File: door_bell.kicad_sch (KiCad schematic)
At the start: 75 parts, among them J1 8-10V AC/DC, J2 Speaker, J3 SWITCH1, J4 Door panel, J5 UART, J6 JTAG, J7 BOOT, J8 MicroSD, K1 HJR 1-2C, Q1 BC338, SW1 Reset, U1 NCP1117-5v, U2 MAX98357A, U3 NCP1117-3v3, U4 DS3231M, U5 MAX3232, U6 ESP32-WROVER-B, U7 74LVC2G14

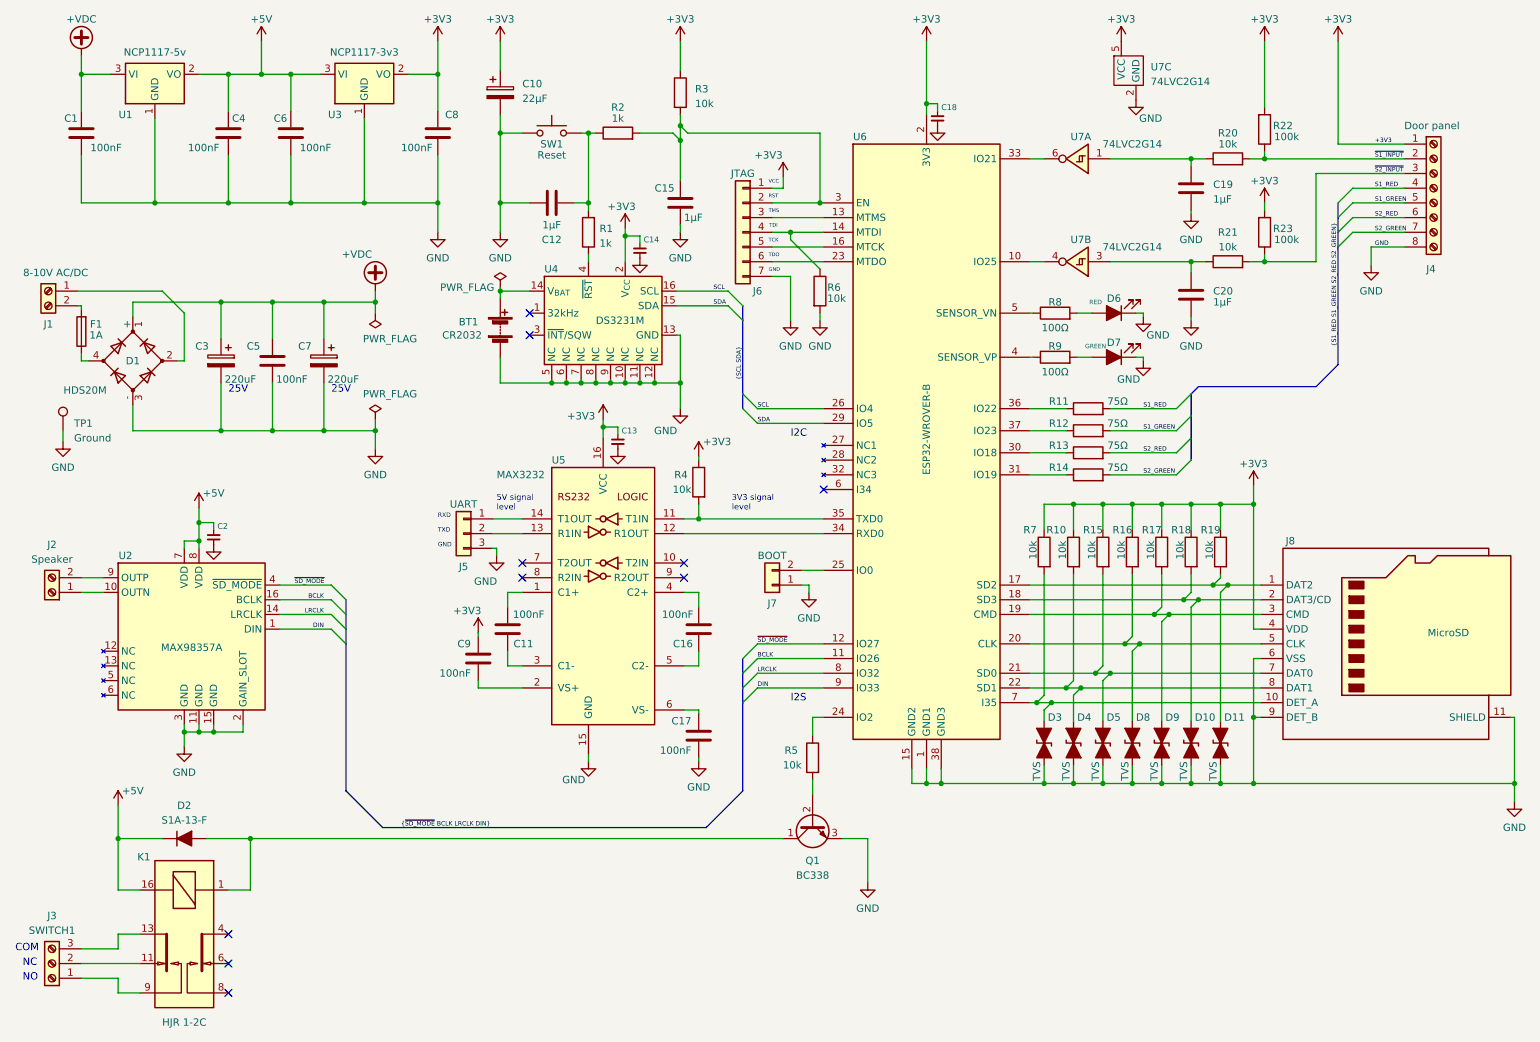
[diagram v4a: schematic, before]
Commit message: GND plane routing
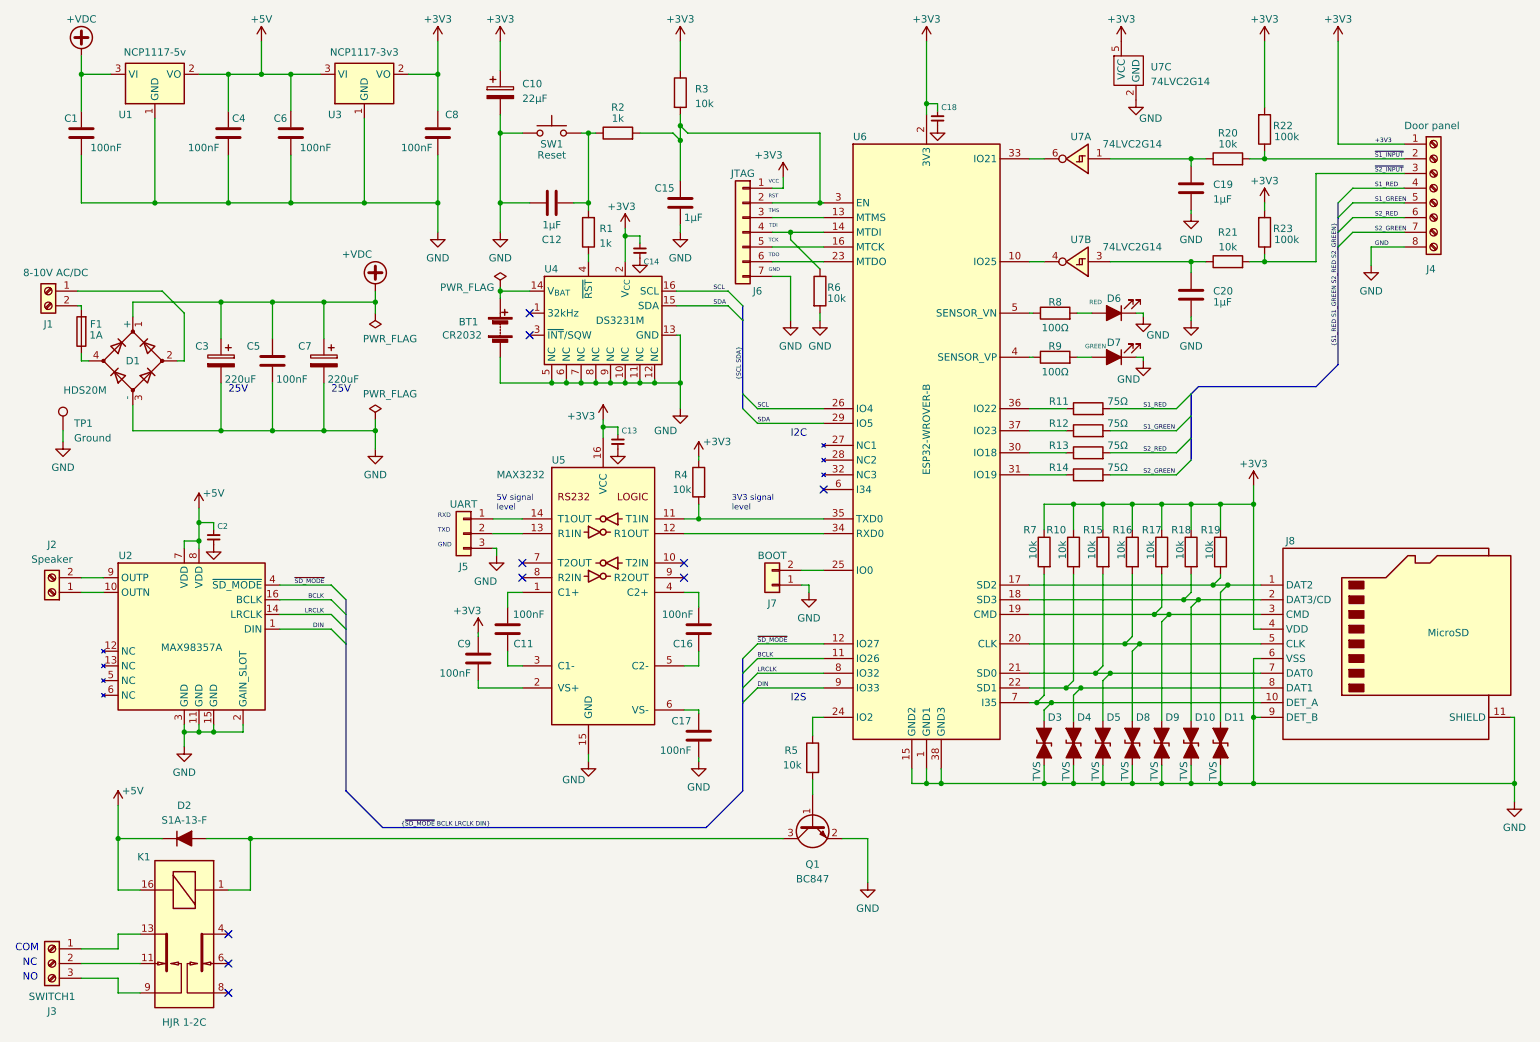
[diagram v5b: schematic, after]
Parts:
- removed Q1: BC338, Package_TO_SOT_THT:TO-92_Inline, symbol Transistor_BJT:BC338
- added Q1: BC847, Package_TO_SOT_SMD:SOT-23, symbol Transistor_BJT:BC847
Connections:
- net +3V3: now also C14.2; no longer C14.1
- net GND: now also C14.1, Q1.2 (E); no longer C14.2
- net at D2.2 (A), K1.1: now also Q1.3 (C)
- net at K1.13: now also J3.1 (Pin_1); no longer J3.3 (Pin_3)
- net at K1.9: now also J3.3 (Pin_3); no longer J3.1 (Pin_1)
- net at R5.2: now also Q1.1 (B)
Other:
- moved on the sheet: J3
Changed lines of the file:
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@@
     )
   )
-  (symbol (lib_id "Connector:Screw_Terminal_01x03") (at 25.4 182.245 180) (unit 1)
-    (in_bom yes) (on_board yes) (dnp no) (fields_autoplaced)
-    (property "Reference" "J3" (at 25.4 173.99 0)
-      (effects (font (size 1.27 1.27)))
-    )
-    (property "Value" "SWITCH1" (at 25.4 176.53 0)
+  (symbol (lib_id "Connector:Screw_Terminal_01x03") (at 25.4 182.245 0) (mirror y) (unit 1)
+    (in_bom yes) (on_board yes) (dnp no)
+    (property "Reference" "J3" (at 25.4 190.5 0)
+      (effects (font (size 1.27 1.27)))
+    )
+    (property "Value" "SWITCH1" (at 25.4 187.96 0)
       (effects (font (size 1.27 1.27)))
     )
@@
         (path "/c78ad4c4-54c1-4b1d-a971-e4b8abed6bf8"
           (reference "R3") (unit 1)
-        )
-      )
-    )
-  )
-  (symbol (lib_id "Transistor_BJT:BC338") (at 156.845 158.115 90) (mirror x) (unit 1)
-    (in_bom yes) (on_board yes) (dnp no) (fields_autoplaced)
-    (property "Reference" "Q1" (at 156.845 164.465 90)
-      (effects (font (size 1.27 1.27)))
-    )
-    (property "Value" "BC338" (at 156.845 167.005 90)
-      (effects (font (size 1.27 1.27)))
-    )
-    (property "Footprint" "Package_TO_SOT_THT:TO-92_Inline" (at 158.75 163.195 0)
-      (effects (font (size 1.27 1.27) italic) (justify left) hide)
-    )
-    (property "Datasheet" "http://diotec.com/tl_files/diotec/files/pdf/datasheets/bc337" (at 156.845 158.115 0)
-      (effects (font (size 1.27 1.27)) (justify left) hide)
-    )
-    (pin "1")
-    (pin "2")
-    (pin "3")
-    (instances
-      (project "door_bell"
-        (path "/c78ad4c4-54c1-4b1d-a971-e4b8abed6bf8"
-          (reference "Q1") (unit 1)
         )
       )
@@
     )
   )
-  (symbol (lib_id "Device_espena:C_Decoupling") (at 127 59.055 0) (unit 1)
-    (in_bom yes) (on_board yes) (dnp no)
-    (property "Reference" "C14" (at 127.635 57.15 0)
+  (symbol (lib_id "Device_espena:C_Decoupling") (at 127 59.055 0) (mirror x) (unit 1)
+    (in_bom yes) (on_board yes) (dnp no)
+    (property "Reference" "C14" (at 127.635 60.96 0)
       (effects (font (size 1 1)) (justify left))
     )
-    (property "Value" "C_Decoupling" (at 127.254 61.087 0)
+    (property "Value" "C_Decoupling" (at 127.254 57.023 0)
       (effects (font (size 1.27 1.27)) (justify left) hide)
     )
@@
         )
       )
+    )
+  )
+  (symbol (lib_id "Transistor_BJT:BC847") (at 156.845 158.115 90) (mirror x) (unit 1)
+    (in_bom yes) (on_board yes) (dnp no) (fields_autoplaced)
+    (property "Reference" "Q1" (at 156.845 165.1 90)
+      (effects (font (size 1.27 1.27)))
+    )
+    (property "Value" "BC847" (at 156.845 167.64 90)
+      (effects (font (size 1.27 1.27)))
+    )
+    (property "Footprint" "Package_TO_SOT_SMD:SOT-23" (at 158.75 163.195 0)
+      (effects (font (size 1.27 1.27) italic) (justify left) hide)
+    )
+    (property "Datasheet" "http://www.infineon.com/dgdl/Infineon-BC847SERIES_BC848SERIES_BC849SERIES_BC850SERIES-DS-v01_01-en.pdf?fileId=db3a304314dca389011541d4630a1657" (at 156.845 158.115 0)
+      (effects (font (size 1.27 1.27)) (justify left) hide)
+    )
+    (pin "1")
+    (pin "2")
+    (pin "3")
+    (instances
+      (project "door_bell"
+        (path "/c78ad4c4-54c1-4b1d-a971-e4b8abed6bf8"
+          (reference "Q1") (unit 1)
+        )
+      )

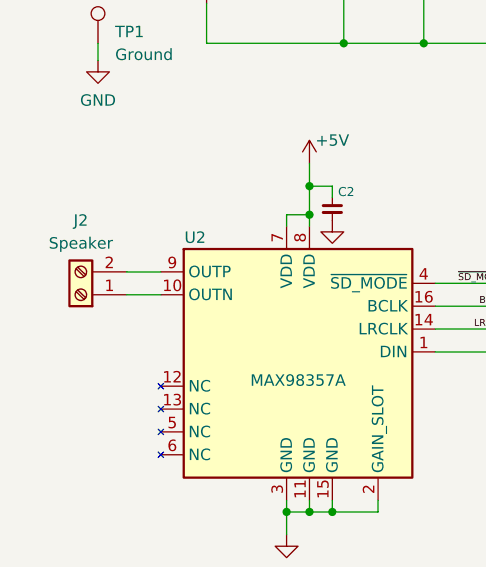
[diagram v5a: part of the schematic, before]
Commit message: Initial routing of power rails and some signals
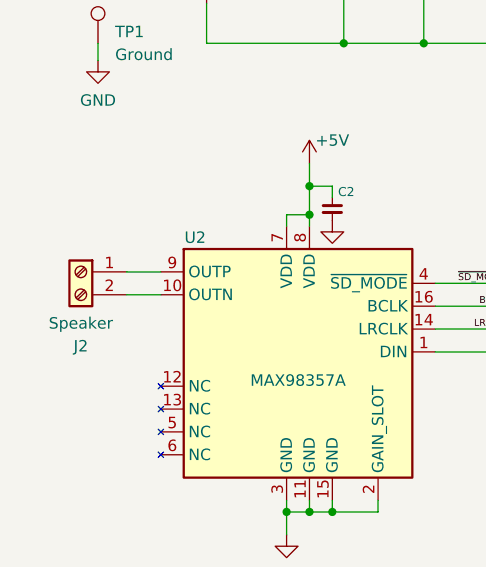
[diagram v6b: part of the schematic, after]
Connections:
- net at J2.1 (Pin_1): now also U2.9 (OUTP); no longer U2.10 (OUTN)
- net at J2.2 (Pin_2): now also U2.10 (OUTN); no longer U2.9 (OUTP)
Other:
- moved on the sheet: J2
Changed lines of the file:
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@@
     )
   )
-  (symbol (lib_id "Connector:Screw_Terminal_01x02") (at 25.4 118.11 180) (unit 1)
-    (in_bom yes) (on_board yes) (dnp no) (fields_autoplaced)
-    (property "Reference" "J2" (at 25.4 109.855 0)
+  (symbol (lib_id "Connector:Screw_Terminal_01x02") (at 25.4 115.57 0) (mirror y) (unit 1)
+    (in_bom yes) (on_board yes) (dnp no)
+    (property "Reference" "J2" (at 25.4 123.825 0)
       (effects (font (size 1.27 1.27)))
     )
-    (property "Value" "Speaker" (at 25.4 112.395 0)
+    (property "Value" "Speaker" (at 25.4 121.285 0)
       (effects (font (size 1.27 1.27)))
     )
-    (property "Footprint" "TerminalBlock_Phoenix:TerminalBlock_Phoenix_PT-1,5-2-3.5-H_1x02_P3.50mm_Horizontal" (at 25.4 118.11 0)
+    (property "Footprint" "TerminalBlock_Phoenix:TerminalBlock_Phoenix_PT-1,5-2-3.5-H_1x02_P3.50mm_Horizontal" (at 25.4 115.57 0)
       (effects (font (size 1.27 1.27)) hide)
     )
-    (property "Datasheet" "~" (at 25.4 118.11 0)
+    (property "Datasheet" "~" (at 25.4 115.57 0)
       (effects (font (size 1.27 1.27)) hide)
     )

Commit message: Done routing
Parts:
- J1, J2: footprint TerminalBlock_Phoenix:TerminalBlock_Phoenix_PT-1,5-2-3.5-H_1x02_P3.50mm_Horizontal -> TerminalBlock_Phoenix_espena:TerminalBlock_Phoenix_PT-1,5-2-3.5-H_1x02_P3.50mm_Horizontal_stackable
- J3: footprint TerminalBlock_Phoenix:TerminalBlock_Phoenix_PT-1,5-3-3.5-H_1x03_P3.50mm_Horizontal -> TerminalBlock_Phoenix_espena:TerminalBlock_Phoenix_PT-1,5-3-3.5-H_1x03_P3.50mm_Horizontal_stackable
- J4: footprint TerminalBlock_Phoenix:TerminalBlock_Phoenix_PT-1,5-8-3.5-H_1x08_P3.50mm_Horizontal -> TerminalBlock_Phoenix_espena:TerminalBlock_Phoenix_PT-1,5-8-3.5-H_1x08_P3.50mm_Horizontal_stackable
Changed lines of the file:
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@@
       (effects (font (size 1.27 1.27)))
     )
-    (property "Footprint" "TerminalBlock_Phoenix:TerminalBlock_Phoenix_PT-1,5-2-3.5-H_1x02_P3.50mm_Horizontal" (at 24.765 66.04 0)
+    (property "Footprint" "TerminalBlock_Phoenix_espena:TerminalBlock_Phoenix_PT-1,5-2-3.5-H_1x02_P3.50mm_Horizontal_stackable" (at 24.765 66.04 0)
       (effects (font (size 1.27 1.27)) hide)
     )
@@
       (effects (font (size 1.27 1.27)) (justify left))
     )
-    (property "Footprint" "TerminalBlock_Phoenix:TerminalBlock_Phoenix_PT-1,5-8-3.5-H_1x08_P3.50mm_Horizontal" (at 264.16 48.26 0)
+    (property "Footprint" "TerminalBlock_Phoenix_espena:TerminalBlock_Phoenix_PT-1,5-8-3.5-H_1x08_P3.50mm_Horizontal_stackable" (at 264.16 48.26 0)
       (effects (font (size 1.27 1.27)) hide)
     )
@@
       (effects (font (size 1.27 1.27)))
     )
-    (property "Footprint" "TerminalBlock_Phoenix:TerminalBlock_Phoenix_PT-1,5-3-3.5-H_1x03_P3.50mm_Horizontal" (at 25.4 182.245 0)
+    (property "Footprint" "TerminalBlock_Phoenix_espena:TerminalBlock_Phoenix_PT-1,5-3-3.5-H_1x03_P3.50mm_Horizontal_stackable" (at 25.4 182.245 0)
       (effects (font (size 1.27 1.27)) hide)
     )
@@
       (effects (font (size 1.27 1.27)))
     )
-    (property "Footprint" "TerminalBlock_Phoenix:TerminalBlock_Phoenix_PT-1,5-2-3.5-H_1x02_P3.50mm_Horizontal" (at 25.4 115.57 0)
-      (effects (font (size 1.27 1.27)) hide)
-    )
+    (property "Footprint" "TerminalBlock_Phoenix_espena:TerminalBlock_Phoenix_PT-1,5-2-3.5-H_1x02_P3.50mm_Horizontal_stackable" (at 25.4 115.57 0)
+      (effects (font (size 1.27 1.27)) hide)
+    )

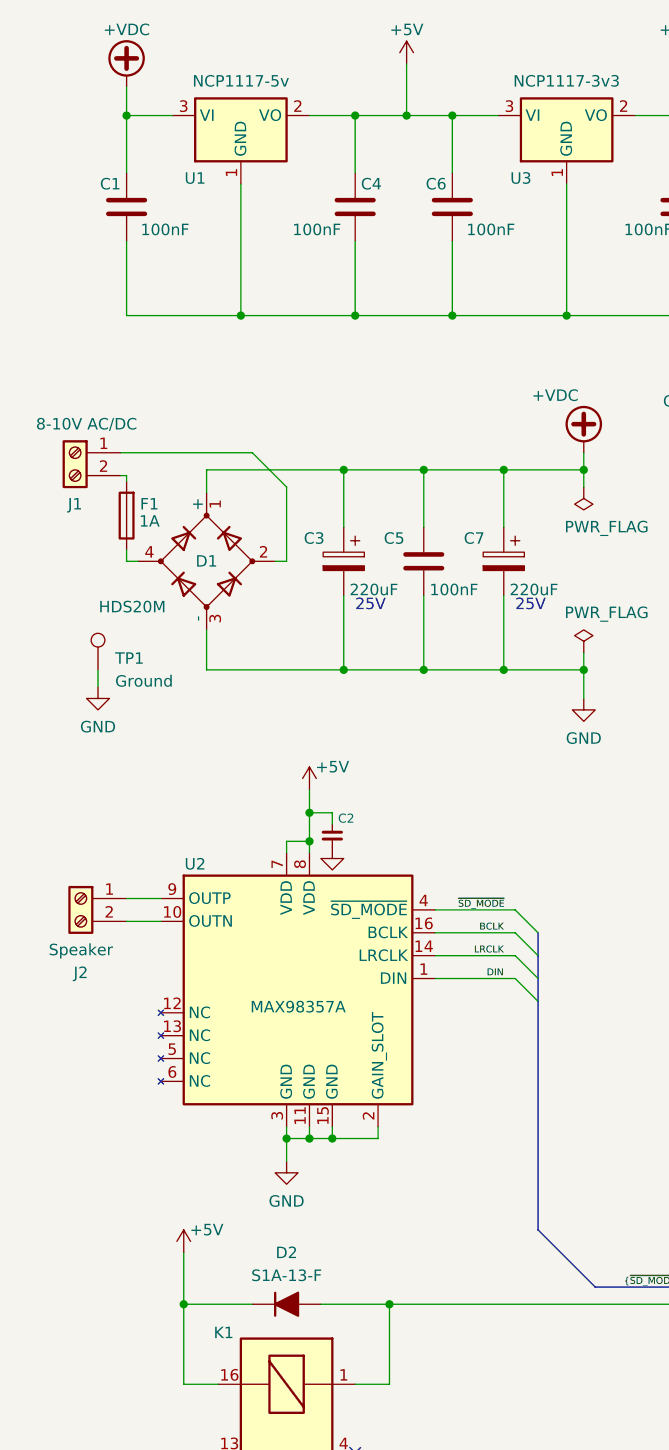
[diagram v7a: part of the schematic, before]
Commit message: Change to alternative voltage regulator types
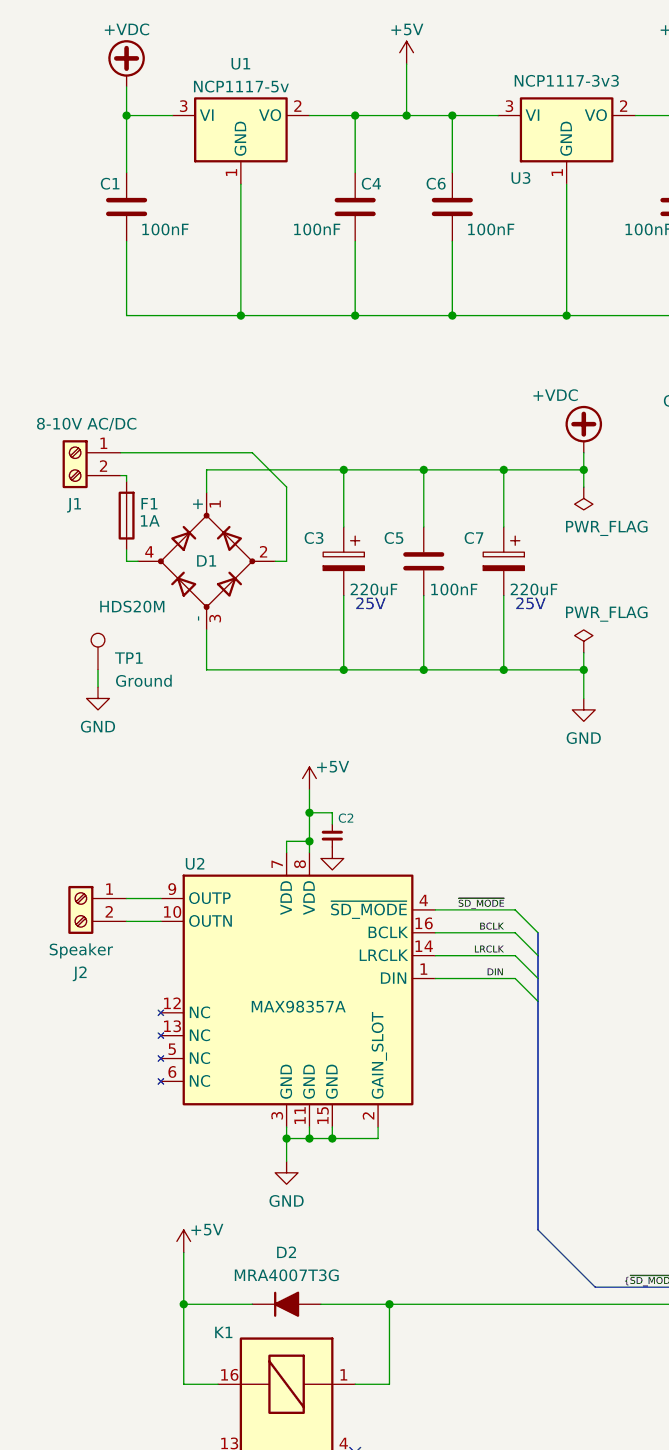
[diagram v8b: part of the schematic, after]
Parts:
- removed U1: NCP1117-5v, Package_TO_SOT_SMD:SOT-223-3_TabPin2, symbol Regulator_Linear:NCP1117-3.3_SOT223
- added U1: NCP1117-5v, Package_TO_SOT_SMD:SOT-223-3_TabPin2, symbol Regulator_Linear:NCP1117-5.0_SOT223
- D2: value S1A-13-F -> MRA4007T3G
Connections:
- net +5V: now also U1.2 (VO)
- net +VDC: now also U1.3 (VI)
- net GND: now also U1.1 (GND)
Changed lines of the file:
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@@
       (effects (font (size 1.27 1.27)))
     )
-    (property "Value" "S1A-13-F" (at 48.26 157.48 0)
+    (property "Value" "MRA4007T3G" (at 48.26 157.48 0)
       (effects (font (size 1.27 1.27)))
     )
@@
         (path "/c78ad4c4-54c1-4b1d-a971-e4b8abed6bf8"
           (reference "R21") (unit 1)
-        )
-      )
-    )
-  )
-  (symbol (lib_id "Regulator_Linear:NCP1117-3.3_SOT223") (at 43.18 28.575 0) (unit 1)
-    (in_bom yes) (on_board yes) (dnp no)
-    (property "Reference" "U1" (at 38.1 35.56 0)
-      (effects (font (size 1.27 1.27)))
-    )
-    (property "Value" "NCP1117-5v" (at 43.18 24.765 0)
-      (effects (font (size 1.27 1.27)))
-    )
-    (property "Footprint" "Package_TO_SOT_SMD:SOT-223-3_TabPin2" (at 43.18 23.495 0)
-      (effects (font (size 1.27 1.27)) hide)
-    )
-    (property "Datasheet" "http://www.onsemi.com/pub_link/Collateral/NCP1117-D.PDF" (at 45.72 34.925 0)
-      (effects (font (size 1.27 1.27)) hide)
-    )
-    (pin "1")
-    (pin "2")
-    (pin "3")
-    (instances
-      (project "door_bell"
-        (path "/c78ad4c4-54c1-4b1d-a971-e4b8abed6bf8"
-          (reference "U1") (unit 1)
         )
       )
@@
         )
       )
+    )
+  )
+  (symbol (lib_id "Regulator_Linear:NCP1117-5.0_SOT223") (at 43.18 28.575 0) (unit 1)
+    (in_bom yes) (on_board yes) (dnp no) (fields_autoplaced)
+    (property "Reference" "U1" (at 43.18 22.86 0)
+      (effects (font (size 1.27 1.27)))
+    )
+    (property "Value" "NCP1117-5v" (at 43.18 25.4 0)
+      (effects (font (size 1.27 1.27)))
+    )
+    (property "Footprint" "Package_TO_SOT_SMD:SOT-223-3_TabPin2" (at 43.18 23.495 0)
+      (effects (font (size 1.27 1.27)) hide)
+    )
+    (property "Datasheet" "http://www.onsemi.com/pub_link/Collateral/NCP1117-D.PDF" (at 45.72 34.925 0)
+      (effects (font (size 1.27 1.27)) hide)
+    )
+    (pin "1")
+    (pin "2")
+    (pin "3")
+    (instances
+      (project "door_bell"
+        (path "/c78ad4c4-54c1-4b1d-a971-e4b8abed6bf8"
+          (reference "U1") (unit 1)
+        )
+      )
